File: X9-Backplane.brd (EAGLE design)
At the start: 122.1 x 93.9 mm, 11 parts

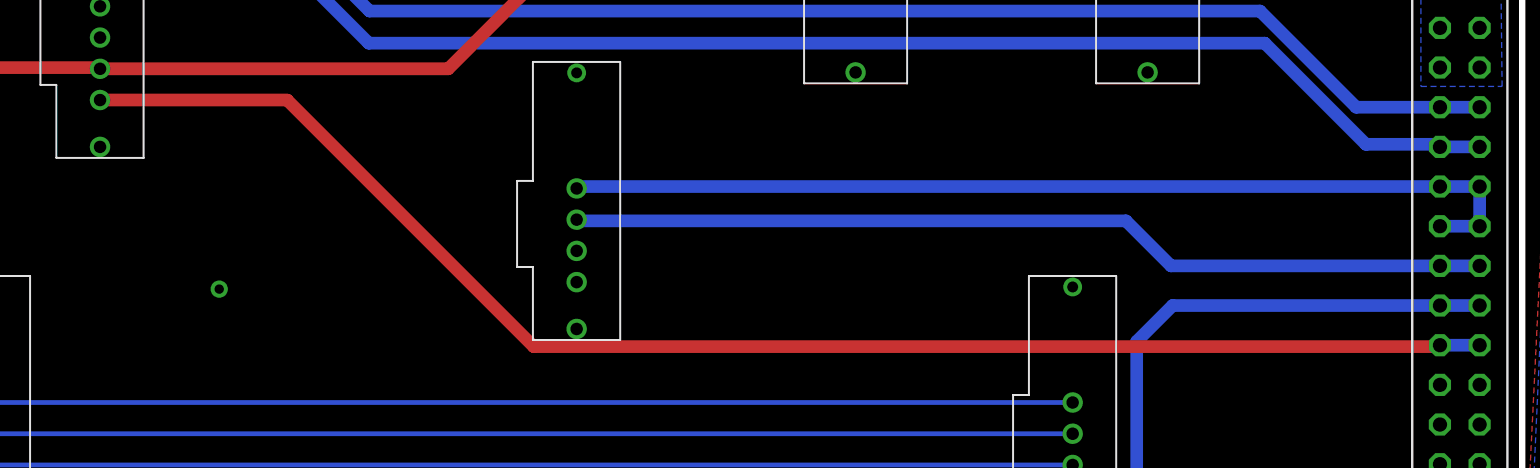
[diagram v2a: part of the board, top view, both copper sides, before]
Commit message: modified 5V_BT_LED on board layout
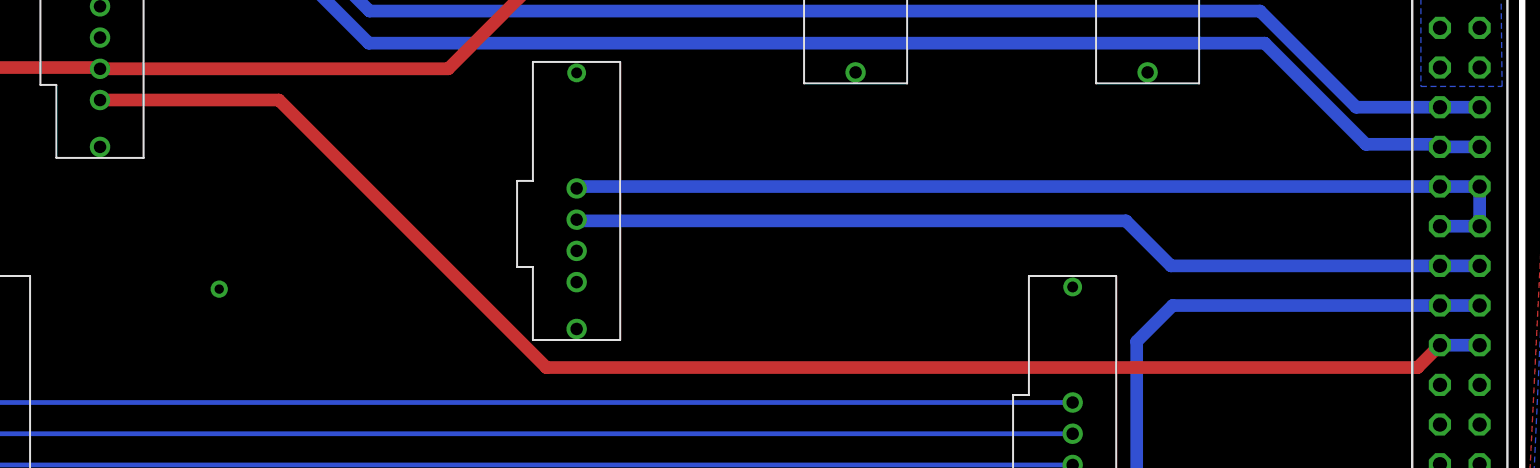
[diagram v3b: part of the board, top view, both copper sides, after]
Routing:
- net 5V_BT_LED: track 94.9 -> 96.0 mm
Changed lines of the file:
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@@
 <grid distance="1" unitdist="mm" unit="mm" style="lines" multiple="1" display="yes" altdistance="0.025" altunitdist="inch" altunit="inch"/>
 <layers>
-<layer number="1" name="Top" color="4" fill="1" visible="no" active="yes"/>
+<layer number="1" name="Top" color="4" fill="1" visible="yes" active="yes"/>
 <layer number="2" name="Route2" color="1" fill="3" visible="no" active="yes"/>
 <layer number="3" name="Route3" color="4" fill="3" visible="no" active="yes"/>
@@
 <layer number="14" name="Route14" color="1" fill="6" visible="no" active="yes"/>
 <layer number="15" name="Route15" color="4" fill="6" visible="no" active="yes"/>
-<layer number="16" name="Bottom" color="1" fill="1" visible="yes" active="yes"/>
+<layer number="16" name="Bottom" color="1" fill="1" visible="no" active="yes"/>
 <layer number="17" name="Pads" color="2" fill="1" visible="yes" active="yes"/>
 <layer number="18" name="Vias" color="2" fill="1" visible="yes" active="yes"/>
@@
 <contactref element="BT_POWER" pad="4"/>
 <wire x1="118.76" y1="26.43" x2="116.22" y2="26.43" width="0.8128" layer="16"/>
-<wire x1="30.4172" y1="42.1294" x2="42.4018" y2="42.1294" width="0.8128" layer="1"/>
-<wire x1="42.4018" y1="42.1294" x2="58.1914" y2="26.3398" width="0.8128" layer="1"/>
-<wire x1="58.1914" y1="26.3398" x2="116.1298" y2="26.3398" width="0.8128" layer="1"/>
-<wire x1="116.1298" y1="26.3398" x2="116.22" y2="26.43" width="0.8128" layer="1"/>
+<wire x1="30.4172" y1="42.1294" x2="41.8706" y2="42.1294" width="0.8128" layer="1"/>
+<wire x1="41.8706" y1="42.1294" x2="59" y2="25" width="0.8128" layer="1"/>
+<wire x1="59" y1="25" x2="114.79" y2="25" width="0.8128" layer="1"/>
+<wire x1="114.79" y1="25" x2="116.22" y2="26.43" width="0.8128" layer="1"/>
 </signal>
 </signals>

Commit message: Modified BT and PS
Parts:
- PS: value T2I -> DF13-4P-1.25DSA; device BACKPLANE:T2I -> con-hirose-df13:DF13-4P-1.25DSA
- moved BT_POWER 12.9 mm to (31.8, 44.0)
- moved PS 7.74 mm to (61.0, 77.6), turned to 90 degrees
- moved BT_SIGNAL 4.57 mm to (20.4, 26.3), turned to 90 degrees
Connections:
- removed net DSCLM: U$1.36
- removed net DSDAM: U$1.38
- removed net DSDAP: U$1.37
- removed net DSDLP: U$1.35
- removed net N$23: POWER.P$4
- removed net N$28: POWER1.P$4
- new net RX_BT: BT_SIGNAL.2, U$1.22
- new net TX_BT: BT_SIGNAL.1, U$1.20
- net 3.3V: now also BT_SIGNAL.4, PS.P$1; no longer BT_POWER.3, PS.3
- net 5V_BT_LED: now also BT_POWER.3
- net GND: now also BT_SIGNAL.3, PS.P$4; no longer PS.4
- net RX_H: no longer BT_SIGNAL.3
- net RX_L: no longer BT_SIGNAL.4
- net SCL: now also PS.P$2; no longer PS.1
- net SDA: now also PS.P$3; no longer PS.2
- net TX_H: no longer BT_SIGNAL.1
- net TX_L: no longer BT_SIGNAL.2
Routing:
- net RX_BT: track 0.00 -> 14.3 mm
- net TX_BT: track 0.00 -> 14.0 mm
- net 5V_BT_LED: track 96.0 -> 88.6 mm
- net 3.3V: track 94.7 -> 89.3 mm
- net 3V3_PIEZO: track 96.7 -> 101.2 mm
- net GND_PIEZO: track 95.0 -> 99.0 mm
- net TX_H: track 114.2 -> 117.7 mm
- net RX_L: track 115.0 -> 113.4 mm
- net TX_L: track 114.2 -> 115.8 mm
- net SDA: track 69.0 -> 67.4 mm
- net SCL: track 69.3 -> 70.3 mm
- net RX_H: track 114.3 -> 114.9 mm
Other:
- board text removed: "PS"

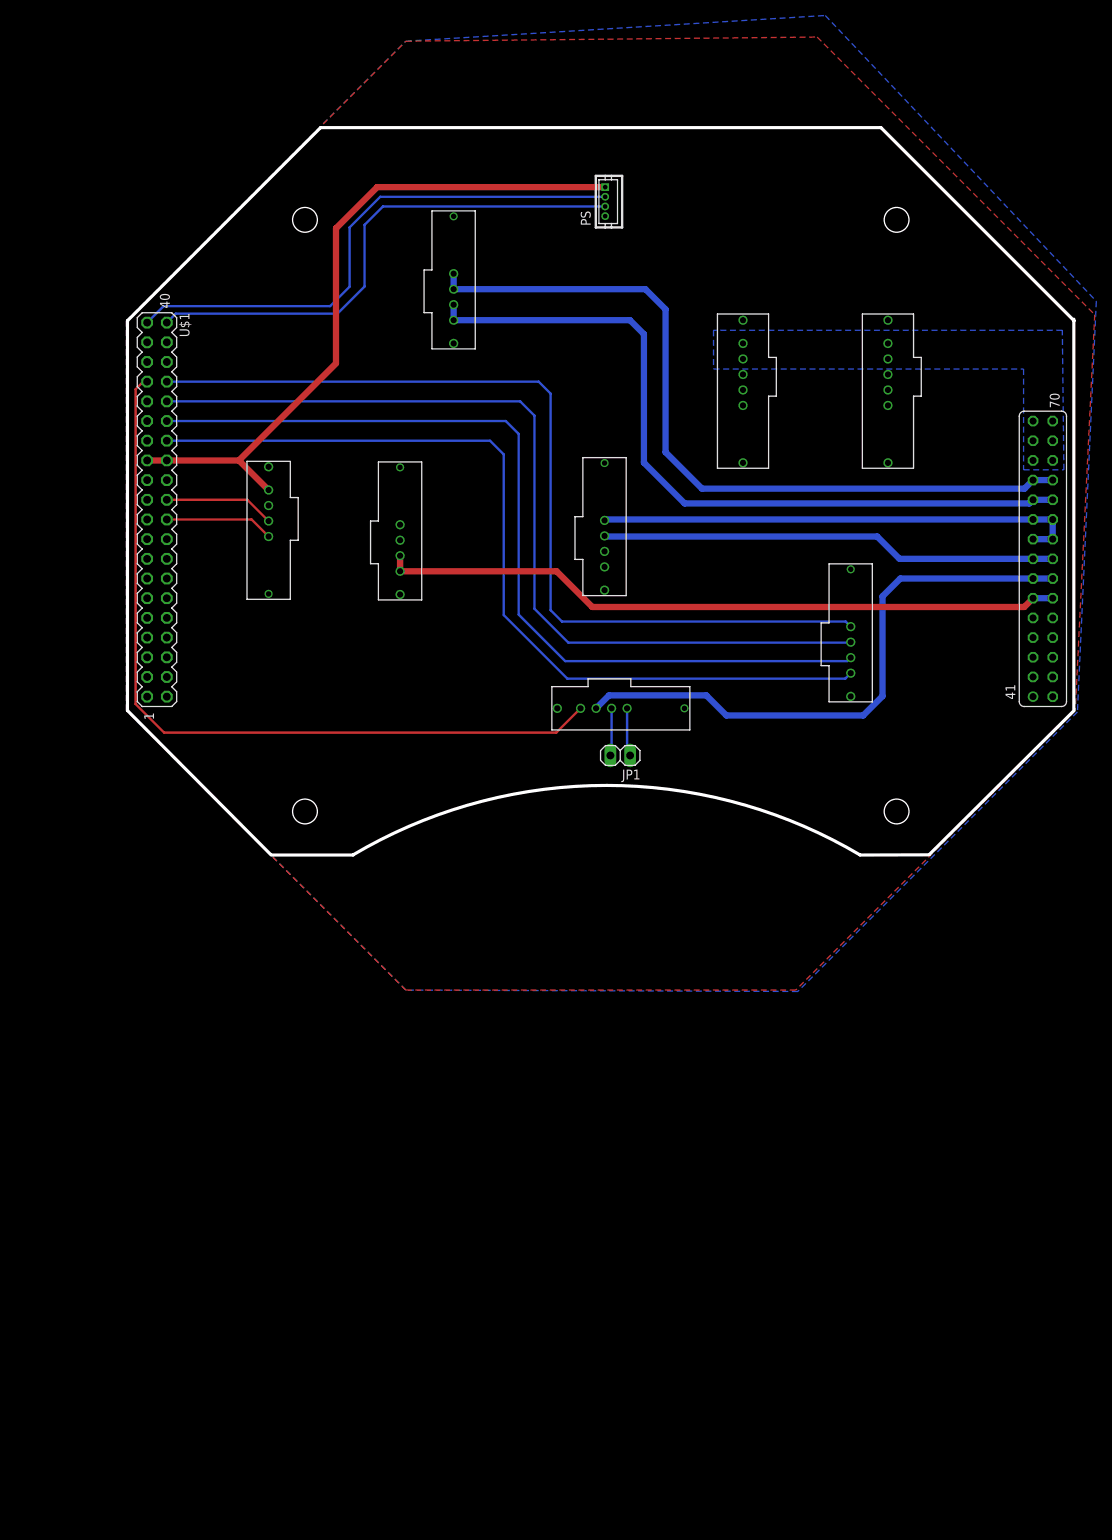
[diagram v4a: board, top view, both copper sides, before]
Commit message: making backplane smaller
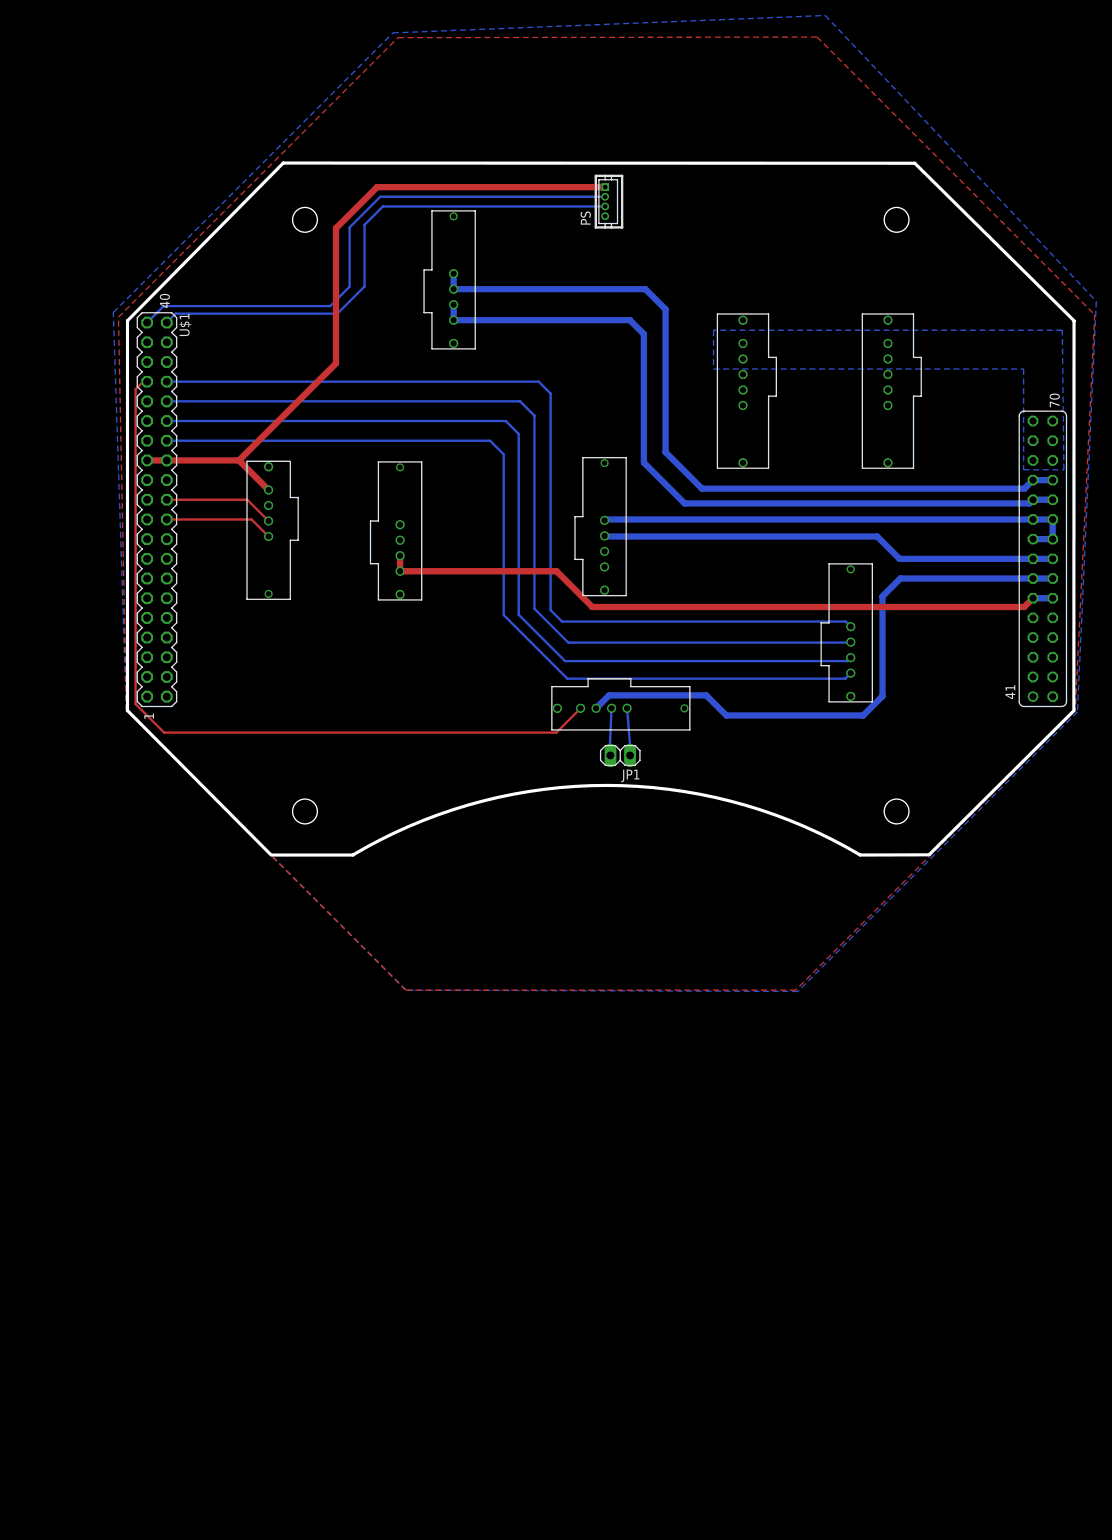
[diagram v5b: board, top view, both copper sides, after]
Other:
- board size 122.1 x 93.9 mm -> 122.1 x 89.3 mm
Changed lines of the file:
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@@
 <hole x="98.616953125" y="75.247665625" drill="3.2"/>
 <circle x="60.45086875" y="37.08158125" radius="73.025" width="0.4064" layer="51"/>
-<wire x1="24.30615" y1="87.14731875" x2="-0.614875" y2="62.22629375" width="0.4064" layer="20"/>
+<wire x1="19.48015" y1="82.57531875" x2="-0.614875" y2="62.22629375" width="0.4064" layer="20"/>
 <wire x1="121.51660625" y1="11.9368625" x2="102.827784375" y2="-6.6519625" width="0.4064" layer="20"/>
 <wire x1="-0.614875" y1="11.9368625" x2="17.87715" y2="-6.6567625" width="0.4064" layer="20"/>
-<wire x1="96.595584375" y1="87.14731875" x2="121.51660625" y2="62.22629375" width="0.4064" layer="20"/>
+<wire x1="100.964384375" y1="82.54991875" x2="121.51660625" y2="62.22629375" width="0.4064" layer="20"/>
 <wire x1="-0.614875" y1="62.22629375" x2="-0.614875" y2="11.9368625" width="0.4064" layer="20"/>
 <text x="84.1" y="63.4" size="1.778" layer="22" rot="MR0">MAIN_POWER</text>
 <text x="103.8" y="63.9" size="1.778" layer="22" rot="MR0">MAIN_POWER</text>
-<wire x1="121.485125" y1="62.42629375" x2="121.485125" y2="12.1368625" width="0.4064" layer="20"/>
+<wire x1="121.510525" y1="62.19769375" x2="121.485125" y2="12.1368625" width="0.4064" layer="20"/>
 <text x="41.8248" y="27.3338" size="1.778" layer="22" rot="MR0">BT_POWER</text>
 <text x="22.5962" y="27.0222" size="1.778" layer="22" rot="MR0">BT_SIGNAL</text>
@@
 <text x="41.2954" y="78.4302" size="1.778" layer="22" rot="MR0">S_PIEZO</text>
 <text x="97.7" y="11.4" size="1.778" layer="22" rot="MR0">SC</text>
-<wire x1="96.595584375" y1="87.14731875" x2="24.30615" y2="87.14731875" width="0.4064" layer="20"/>
+<wire x1="100.964384375" y1="82.54991875" x2="19.48015" y2="82.57531875" width="0.4064" layer="20"/>
 <wire x1="28.496384375" y1="-6.70388125" x2="17.95795" y2="-6.70388125" width="0.4064" layer="20"/>
 <wire x1="102.791384375" y1="-6.67848125" x2="93.90395" y2="-6.70388125" width="0.4064" layer="20"/>
@@
 <signal name="GND">
 <polygon width="0.4064" layer="16" rank="6">
-<vertex x="35.306" y="98.298"/>
+<vertex x="33.6296" y="99.3648"/>
 <vertex x="89.4158" y="101.6126"/>
 <vertex x="124.3838" y="64.7446"/>
@@
 <vertex x="35.306" y="-24.13"/>
 <vertex x="-0.762" y="11.938"/>
-<vertex x="-0.762" y="62.23"/>
+<vertex x="-2.4384" y="63.2968"/>
 </polygon>
 <polygon width="0.4064" layer="1" rank="6">
-<vertex x="-0.762" y="62.23"/>
-<vertex x="35.306" y="98.298"/>
+<vertex x="-1.778" y="62.6872"/>
+<vertex x="34.29" y="98.7552"/>
 <vertex x="88.3666" y="98.8314"/>
 <vertex x="124.1806" y="63.0174"/>
@@
 <contactref element="CAMDATA" pad="1"/>
 <contactref element="JP1" pad="1"/>
-<wire x1="63.843" y1="12.2232" x2="63.843" y2="7.2426" width="0.3048" layer="16"/>
-<wire x1="63.843" y1="7.2426" x2="64.2318" y2="6.1426" width="0.3048" layer="16"/>
+<wire x1="63.843" y1="12.2232" x2="64.2494" y2="7.1918" width="0.3048" layer="16"/>
+<wire x1="64.2494" y1="7.1918" x2="64.2318" y2="6.1426" width="0.3048" layer="16"/>
 </signal>
 <signal name="D-">
 <contactref element="CAMDATA" pad="2"/>
 <contactref element="JP1" pad="2"/>
-<wire x1="61.843" y1="12.2232" x2="61.843" y2="6.4716" width="0.3048" layer="16"/>
-<wire x1="61.843" y1="6.4716" x2="61.6918" y2="6.1426" width="0.3048" layer="16"/>
+<wire x1="61.843" y1="12.2232" x2="61.589" y2="6.6494" width="0.3048" layer="16"/>
+<wire x1="61.589" y1="6.6494" x2="61.6918" y2="6.1426" width="0.3048" layer="16"/>
 </signal>
 <signal name="5V_LED">

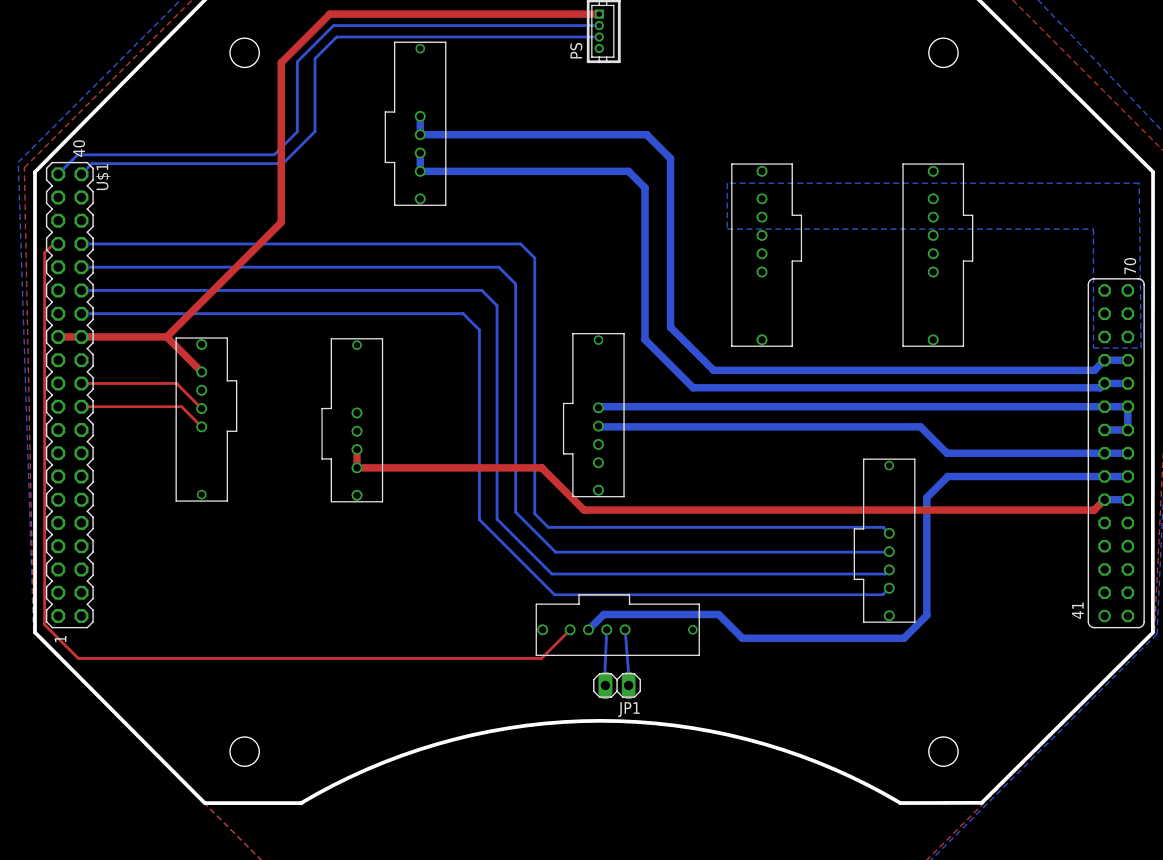
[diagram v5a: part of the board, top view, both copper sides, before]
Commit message: rearanging physical layout
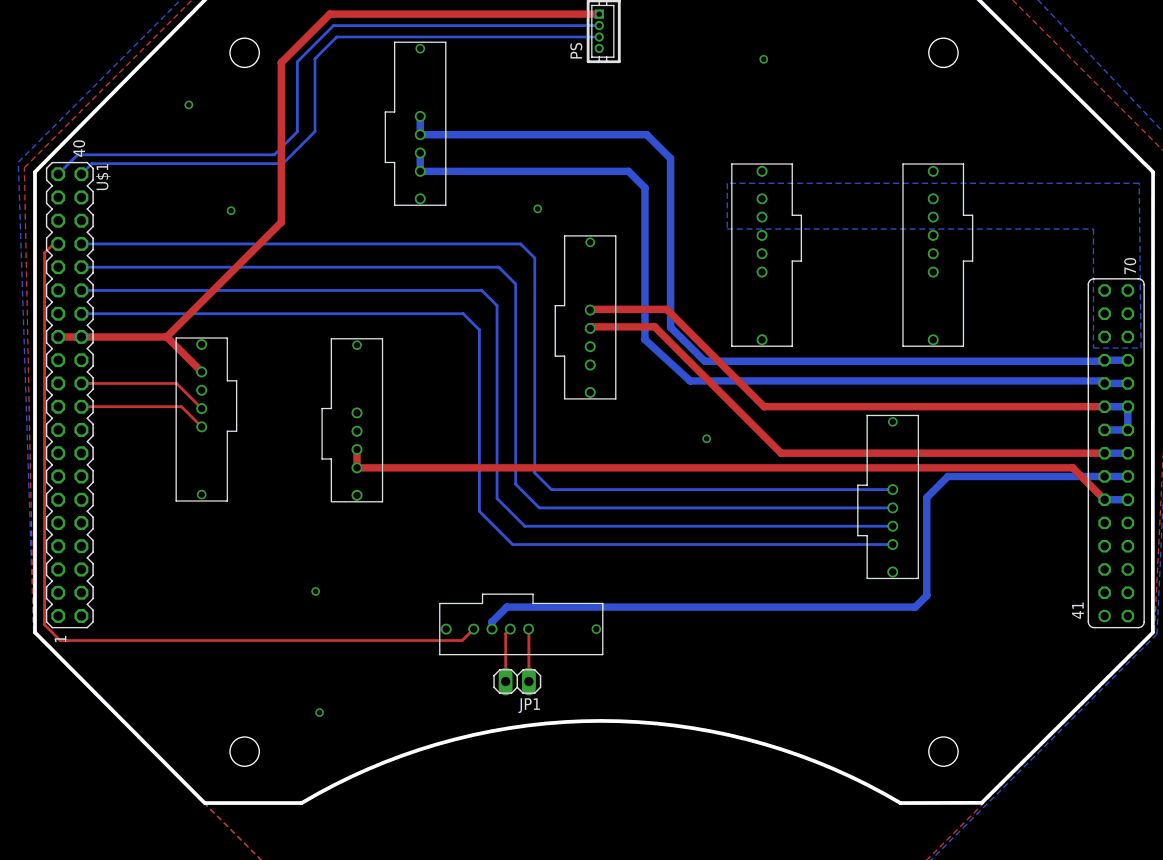
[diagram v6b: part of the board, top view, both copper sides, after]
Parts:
- moved JP1 10.9 mm to (52.1, 6.57)
- moved CAMPOW 10.7 mm to (57.2, 55.2)
- moved CAMDATA 10.5 mm to (61.4, 15.1)
- moved SC 4.79 mm to (90.3, 35.6)
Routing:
- net SERVO_PWM: track 102.7 -> 90.6 mm
- net 5V_LED: track 75.5 -> 83.1 mm
- net 5V_LASER: track 59.0 -> 64.5 mm
- net 5V_CAMERA_TUBE: track 63.0 -> 68.2 mm
- net TX_H: track 117.7 -> 113.5 mm
- net TX_L: track 115.8 -> 112.3 mm
- net RX_H: track 114.9 -> 111.6 mm
- net RX_L: track 113.4 -> 110.7 mm
- net 5V_BT_LED: track 88.6 -> 87.6 mm
- net 3V3_PIEZO: track 101.2 -> 100.4 mm
- net GND_PIEZO: track 99.0 -> 98.5 mm
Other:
- outline, holes or cut-outs redrawn
